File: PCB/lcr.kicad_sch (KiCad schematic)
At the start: 51 parts, among them J1 Conn_01x04_Pin, J2 USB_C_Receptacle_USB2.0_14P, SW1 SW_Push, SW2 SW_Push, U2 TLV75801PDBV, U5 STM32G431CBT6, U8 TLV757P, U9 USBLC6-2SC6, Y2 8 MHz

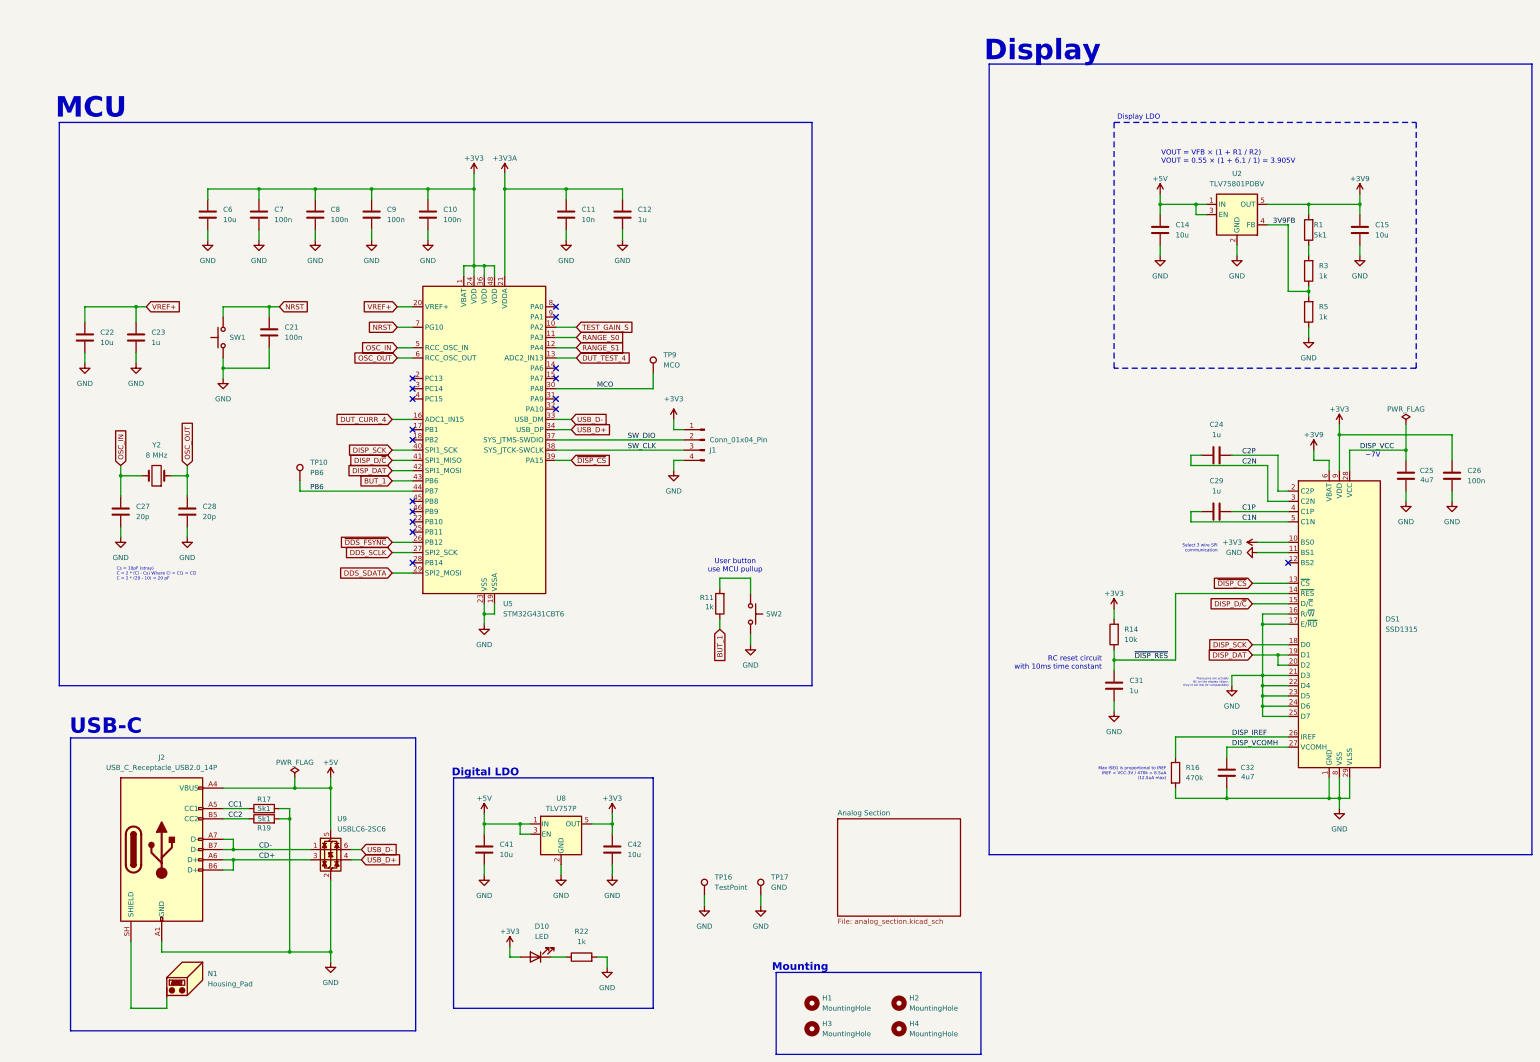
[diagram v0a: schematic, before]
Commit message: Added soft-start
Also added new case step files
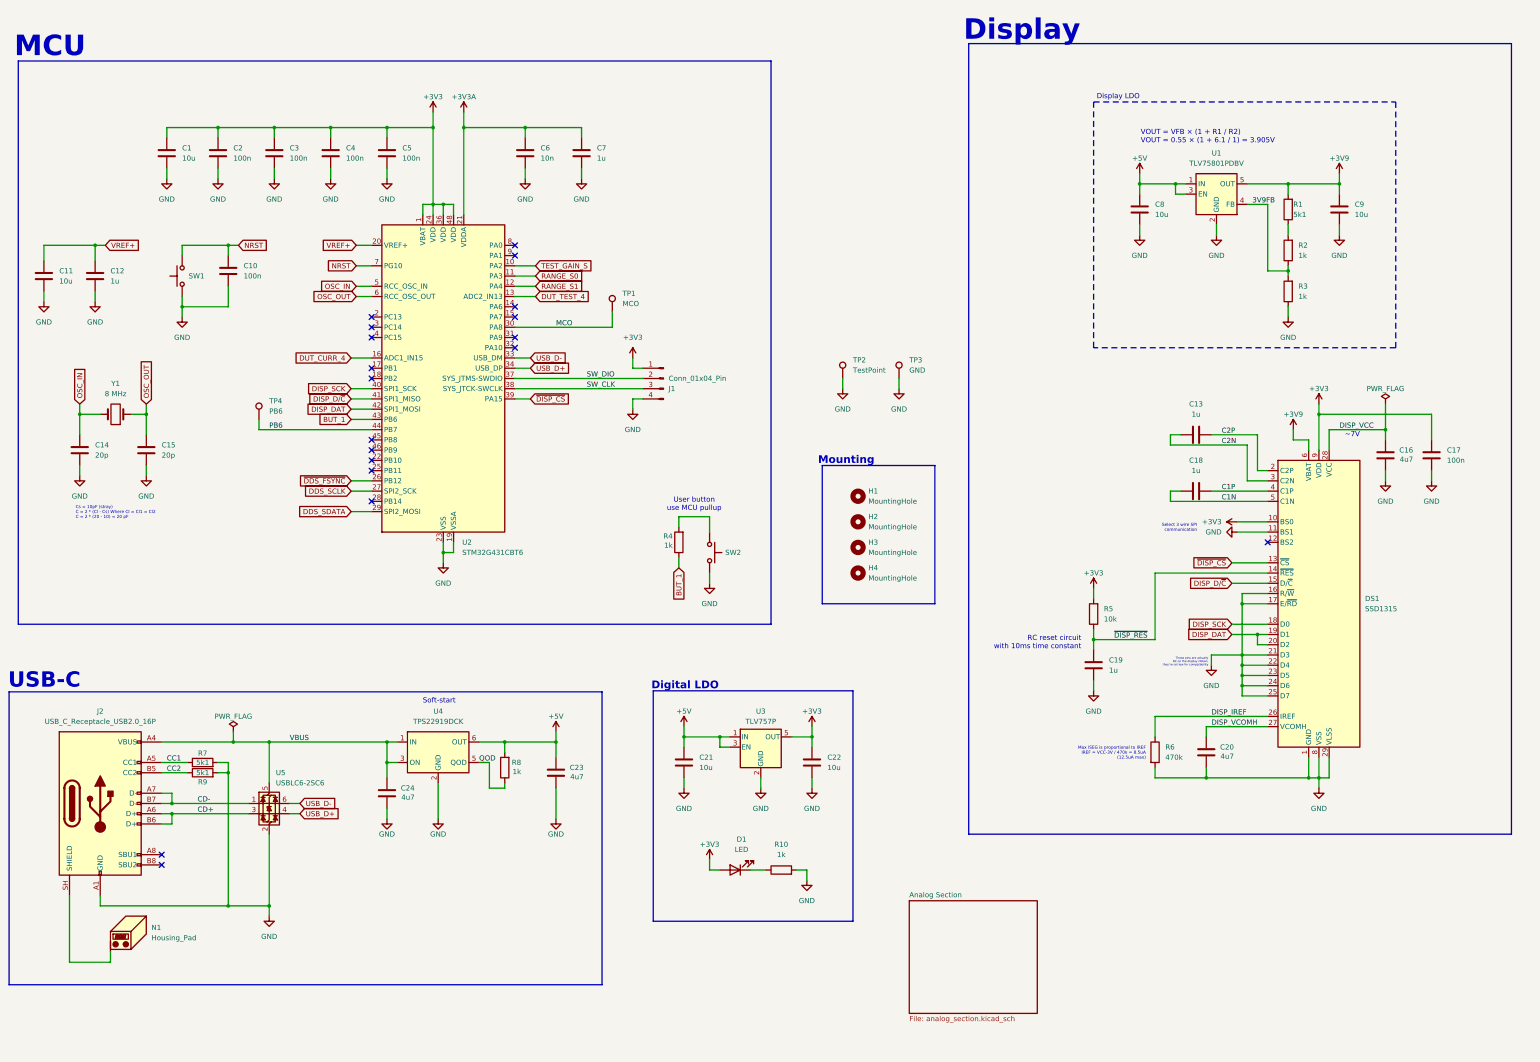
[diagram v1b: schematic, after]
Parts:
- removed J2: USB_C_Receptacle_USB2.0_14P, CustomFootprints:USB_TYPE-C-31-M-12, symbol Connector:USB_C_Receptacle_USB2.0_14P
- added C23, C24: 4u7, Capacitor_SMD:C_0603_1608Metric, symbol Device:C
- added J2: USB_C_Receptacle_USB2.0_16P, CustomFootprints:USB_TYPE-C-31-M-12, symbol Connector:USB_C_Receptacle_USB2.0_16P
- added R8: 1k, Resistor_SMD:R_0603_1608Metric, symbol Device:R
- added U4: TPS22919DCK, Package_TO_SOT_SMD:SOT-363_SC-70-6, symbol Power_Management:TPS22919DCK
- renumbered C6 to C1, C21 to C10, C22 to C11, C23 to C12, C24 to C13, C27 to C14, C28 to C15, C25 to C16, C26 to C17, C29 to C18, C31 to C19, C7 to C2, C32 to C20, C41 to C21, C42 to C22, C8 to C3, C9 to C4, C10 to C5, C11 to C6, C12 to C7, C14 to C8, C15 to C9, D10 to D1, H3 to H2, H2 to H3, R22 to R10, R3 to R2, R5 to R3, R11 to R4, R14 to R5, R16 to R6, R17 to R7, R19 to R9, TP9 to TP1, TP16 to TP2, TP17 to TP3, TP10 to TP4, U2 to U1, U5 to U2, U8 to U3, U9 to U5, Y2 to Y1
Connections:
- net +5V: now also C23.1, R8.2, U4.6 (OUT); no longer U5.5 (VBUS)
- net CC1: now also J2.A5 (CC1)
- net CC2: now also J2.B5 (CC2)
- net CD+: now also J2.A6 (D+), J2.B6 (D+)
- net CD-: now also J2.A7 (D-), J2.B7 (D-)
- net GND: now also C23.2, C24.2, J2.A1 (GND), J2.A12 (GND), J2.B1 (GND), J2.B12 (GND), U4.2 (GND)
- net at N1.1 (PAD): now also J2.SH (SHIELD)
- new net QOD: R8.1, U4.5 (QOD)
- new net VBUS: C24.1, J2.A4 (VBUS), J2.A9 (VBUS), J2.B4 (VBUS), J2.B9 (VBUS), U4.1 (IN), U4.3 (ON), U5.5 (VBUS)
- no-connect marks 17 -> 19
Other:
- note added: "Soft-start"
- moved on the sheet: C1, C10, C11, C12, C13, C14, C15, C16, C17, C18, C19, C2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
